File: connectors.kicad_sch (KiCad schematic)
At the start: 10 parts, among them J3 09665526612, J5 5747841-4

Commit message: edit README.md
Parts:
- removed J3: 09665526612, lib:09665526612, symbol Connector_Generic_Shielded:Conn_01x50_Shielded
- added J3: 5747841-4, lib:57478414, symbol Connector:DA15_Pins_MountingHoles
- renumbered J5 to J4
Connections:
- net +15VA: now also J3.8
- net -15VA: now also J3.1
- net BPIO0: now also J4.6; no longer J4.14 (P14)
- net BPIO1: now also J4.13 (P13); no longer J4.6
- net BPIO2: now also J4.12 (P12); no longer J4.13 (P13)
- net BPIO3: now also J4.4; no longer J4.5
- net BPIO4: now also J4.3; no longer J4.12 (P12)
- net BPIO5: now also J4.10 (P10); no longer J4.4
- net BPIO6: now also J4.9 (P9); no longer J4.11 (P111)
- net BPIO7: now also J4.1; no longer J4.3
- net GND: now also J4.11 (P111), J4.14 (P14), J4.5, J3.0 (PAD), J3.12 (P12), J3.15 (P15), J3.3, J3.6, J3.9 (P9); no longer J4.1, J4.10 (P10), J4.9 (P9)
- net IN0+: now also J3.10 (P10)
- net IN0-: now also J3.2
- net IN1+: now also J3.4
- net IN1-: now also J3.11 (P111)
- net IN2+: now also J3.13 (P13)
- net IN2-: now also J3.5
- net IN3+: now also J3.7
- net IN3-: now also J3.14 (P14)
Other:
- note added: "Backplane"
- note added: "To Detector"
- company: (none) -> NOIRLab
- title: (none) -> 4 channel ADC Module
- moved on the sheet: J4, R129, R130, R131, R132, R133, R134, R135, R136

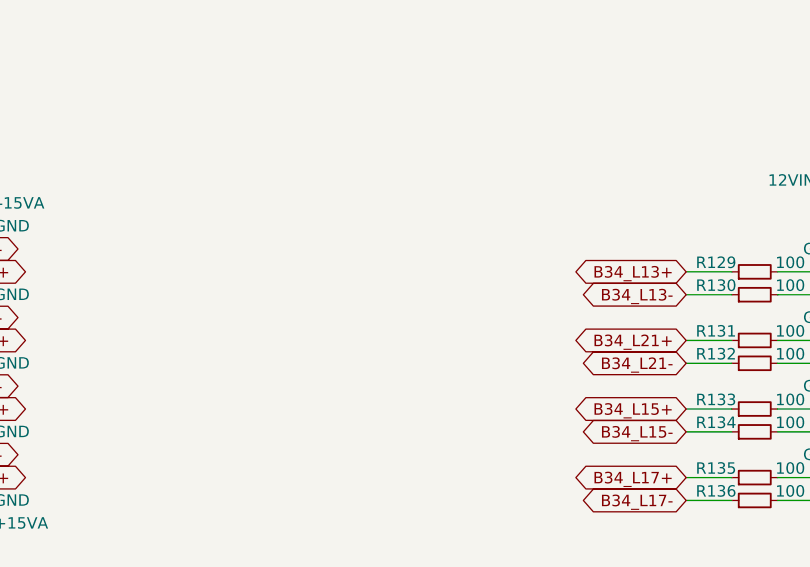
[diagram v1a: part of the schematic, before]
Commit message: Remove floating resistor and reorder schematic pages
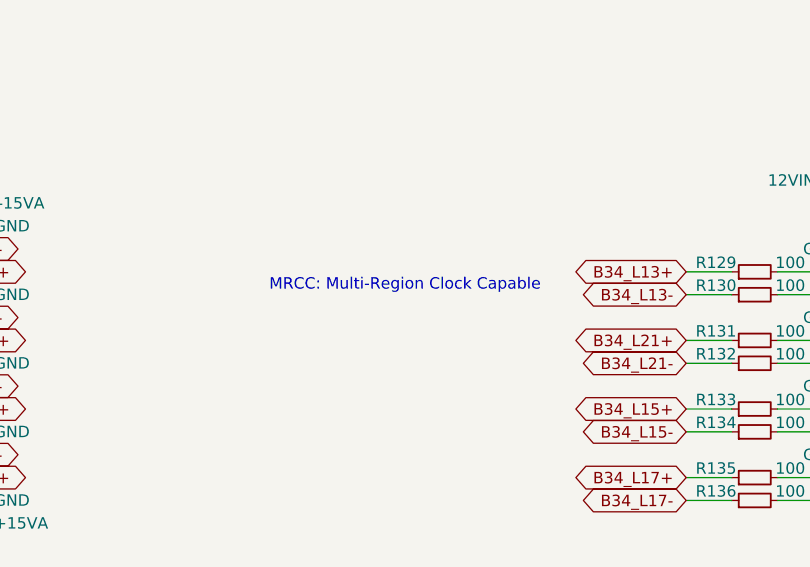
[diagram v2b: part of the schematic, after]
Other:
- note added: "MRCC: Multi-Region Clock Capable"
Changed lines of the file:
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@@
+		)
+	)
+	(text "MRCC: Multi-Region Clock Capable"
+		(exclude_from_sim no)
+		(at 152.908 90.424 0)
+		(effects
+			(font
+				(size 1.27 1.27)
+			)
 		)
 	)
@@
 			(project "adc_board_prot"
 				(path "/c6949a33-abae-4c95-a3fe-c6f7de9ef0a5/ee326142-a1ab-40dd-8d19-bfec08848fdc"
-					(page "17")
+					(page "22")
 				)
 			)
@@
 			(project "adc_board_prot"
 				(path "/c6949a33-abae-4c95-a3fe-c6f7de9ef0a5/ee326142-a1ab-40dd-8d19-bfec08848fdc"
-					(page "16")
+					(page "21")
 				)
 			)
@@
 			(project "adc_board_prot"
 				(path "/c6949a33-abae-4c95-a3fe-c6f7de9ef0a5/ee326142-a1ab-40dd-8d19-bfec08848fdc"
-					(page "5")
-				)
-			)
+					(page "20")
+				)
+			)

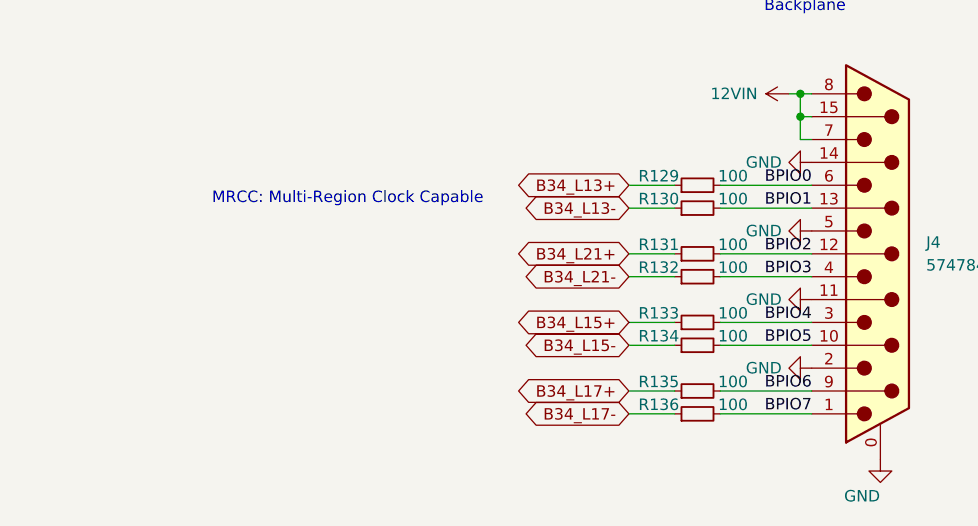
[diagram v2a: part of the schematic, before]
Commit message: Added clock sync and fix minor errors.
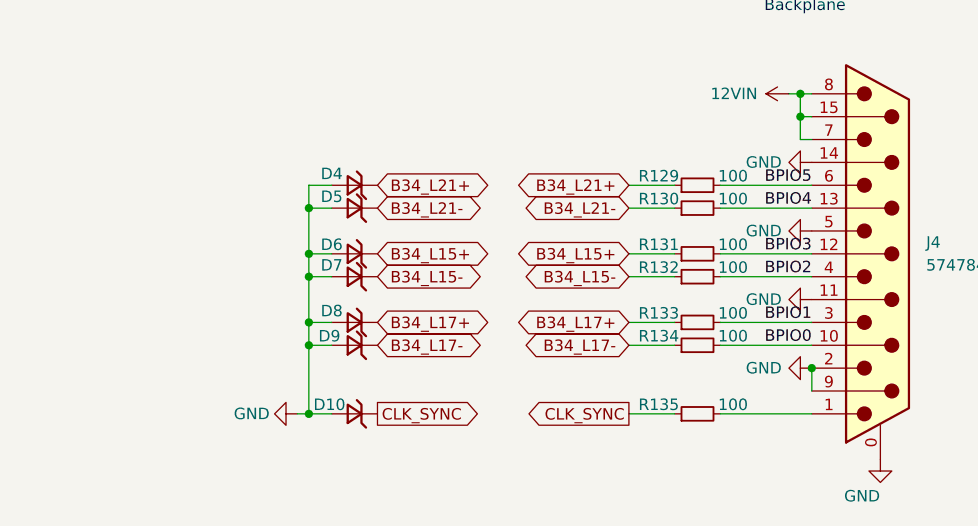
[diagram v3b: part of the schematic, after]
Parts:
- removed R136: 100, Resistor_SMD:R_0402_1005Metric, symbol Device:R_Small
- added D10, D4, D5, D6, D7, D8, D9: ~, lib:TVS_0402_1005Metric, symbol lib:uni_tvs
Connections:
- net B34_L13+ is gone; now on net B34_L21+: R129.1
- net B34_L13- is gone; now on net B34_L21-: R130.1
- net BPIO7 is gone; now on an unnamed net: J4.1
- net B34_L15+: now also R131.1, D6.1 (K); no longer R133.1
- net B34_L15-: now also R132.1, D7.1 (K); no longer R134.1
- net B34_L17+: now also R133.1, D8.1 (K); no longer R135.1
- net B34_L17-: now also R134.1, D9.1 (K)
- net B34_L21+: now also D4.1 (K); no longer R131.1
- net B34_L21-: now also D5.1 (K); no longer R132.1
- net BPIO0: now also J4.10 (P10), R134.2; no longer J4.6, R129.2
- net BPIO1: now also J4.3, R133.2; no longer J4.13 (P13), R130.2
- net BPIO2: now also J4.4, R132.2; no longer J4.12 (P12), R131.2
- net BPIO3: now also J4.12 (P12), R131.2; no longer J4.4, R132.2
- net BPIO4: now also J4.13 (P13), R130.2; no longer J4.3, R133.2
- net BPIO5: now also J4.6, R129.2; no longer J4.10 (P10), R134.2
- net GND: now also J4.9 (P9), D10.2 (A), D4.2 (A), D5.2 (A), D6.2 (A), D7.2 (A), D8.2 (A), D9.2 (A)
- net BPIO6: no longer names the net of R135.2
- net BPIO6: no longer J4.9 (P9)
- new net CLK_SYNC: D10.1 (K), R135.1
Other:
- note removed: "MRCC: Multi-Region Clock Capable"
- moved on the sheet: R135

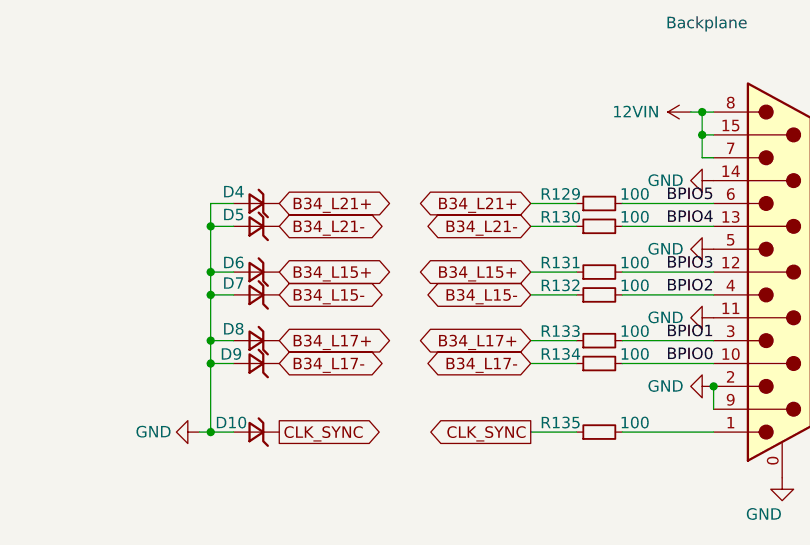
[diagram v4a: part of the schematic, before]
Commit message: Split DC DC schematic and improve layout
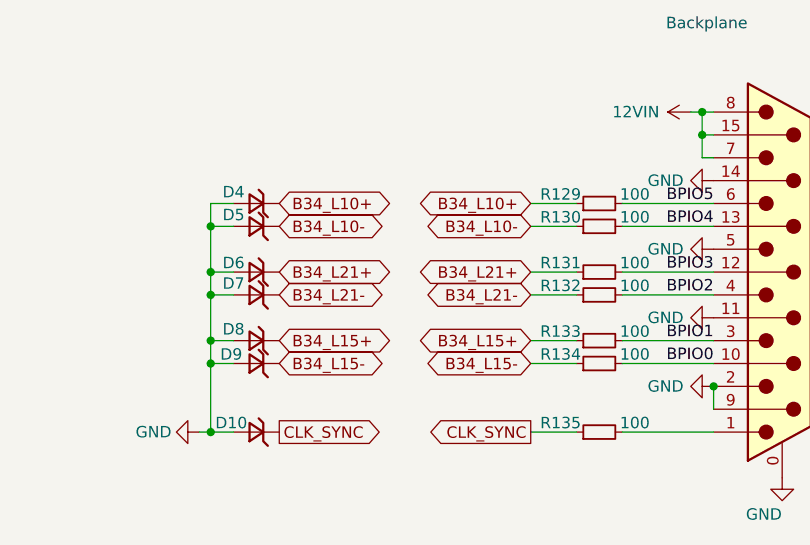
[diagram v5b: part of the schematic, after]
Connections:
- net B34_L17+ is gone; now on net B34_L15+: D8.1 (K), R133.1
- net B34_L17- is gone; now on net B34_L15-: D9.1 (K), R134.1
- net B34_L15+: no longer D6.1 (K), R131.1
- net B34_L15-: no longer D7.1 (K), R132.1
- net B34_L21+: now also D6.1 (K), R131.1; no longer D4.1 (K), R129.1
- net B34_L21-: now also D7.1 (K), R132.1; no longer D5.1 (K), R130.1
- new net B34_L10+: D4.1 (K), R129.1
- new net B34_L10-: D5.1 (K), R130.1

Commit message: Major schematic and PCB changes and latex manual creation.
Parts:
- removed D10, D4, D5, D6, D7, D8, D9: ~, lib:TVS_0402_1005Metric, symbol lib:uni_tvs
- removed R132, R133, R134, R135: 100, Resistor_SMD:R_0402_1005Metric, symbol Device:R_Small
- added C184, C185: 0.1uF, Capacitor_SMD:C_0402_1005Metric, symbol Device:C_Small
- added U29: SN74AXC8T245-Q1, Package_SO:TSSOP-24_4.4x7.8mm_P0.65mm, symbol lib:SN74AXC8T245-Q1
- R129, R130, R131: value 100 -> 10k; footprint Resistor_SMD:R_0402_1005Metric -> Resistor_SMD:R_0603_1608Metric; MPN CRCW0402100RFKEDHP -> CRCW060310K0FKEA
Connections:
- net B34_L10- is gone; now on net 3V3D: R130.1
- net B34_L21+ is gone; now on net 3V3D: R131.1
- net CLK_SYNC: now also U29.21 (B1)
- net GND: now also C184.2, C185.2, U29.12 (GND), U29.13 (GND); no longer J4.9 (P9)
- net BPI0: now reaches J4.1
- net BPI0: now also U29.3 (A1)
- net B34_L10+ renamed 3V3D
- net 3V3D: now also C185.1, U29.1 (V_{CCA})
- net BPIO0 renamed BPI2
- net BPI2: now also U29.5 (A3)
- net BPIO1 renamed BPI3
- net BPI3: now also U29.6 (A4)
- net BPIO2 renamed BPO0
- net BPO0: now also U29.7 (A5)
- net BPIO3: no longer names the net of R131.2
- net BPIO3: now also U29.11 (DIR2); no longer J4.12 (P12)
- net BPIO4: no longer names the net of R130.2
- net BPIO4: now also U29.2 (DIR1); no longer J4.13 (P13)
- net BPIO5 renamed B34_M22
- net B34_M22: now also U29.22 (~{OE}); no longer J4.6
- new net 2V5D: C184.1, U29.23 (V_{CCB}), U29.24 (V_{CCB})
- new net B34_L21: U29.16 (B6)
- new net B34_L22: U29.17 (B5)
- new net B34_M21: U29.20 (B2)
- new net B34_P17: U29.14 (B8)
- new net B34_P18: U29.15 (B7)
- new net B34_T16: U29.18 (B4)
- new net B34_T17: U29.19 (B3)
- new net BPI1: J4.9 (P9), U29.4 (A2)
- new net BPO1: J4.12 (P12), U29.8 (A6)
- new net BPO2: J4.13 (P13), U29.9 (A7)
- new net BPO3: J4.6, U29.10 (A8)
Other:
- moved on the sheet: J3, J4
